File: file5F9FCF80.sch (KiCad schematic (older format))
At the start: 4 parts, among them J5 Conn_01x02, J6 Conn_01x02

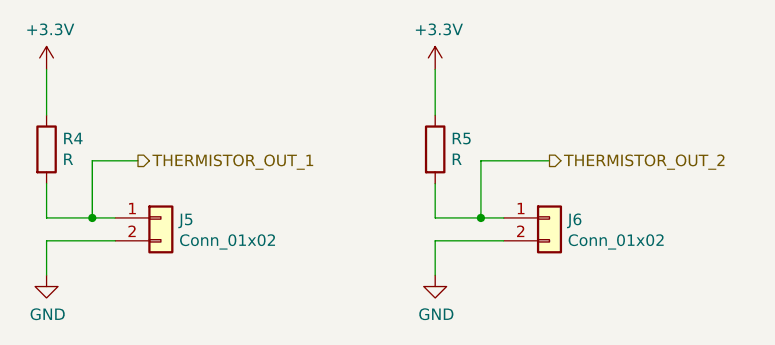
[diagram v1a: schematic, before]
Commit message: Added footprints
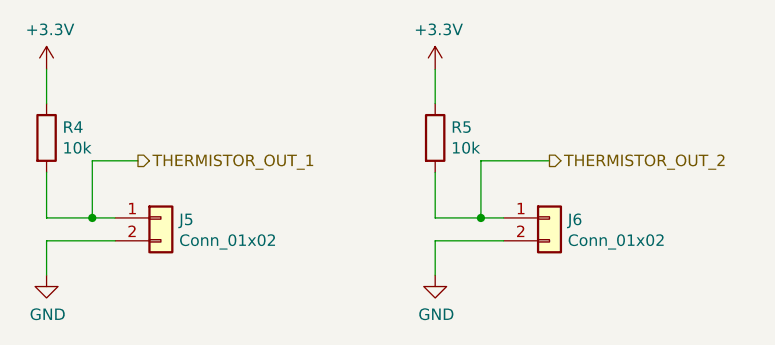
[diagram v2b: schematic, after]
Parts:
- J5, J6: footprint (none) -> Connector_PinHeader_2.54mm:PinHeader_1x02_P2.54mm_Vertical
- R4, R5: value R -> 10k; footprint (none) -> Resistor_SMD:R_0805_2012Metric
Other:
- moved on the sheet: R4, R5
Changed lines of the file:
@@
 L Device:R R4
 U 1 1 5F9FD435
-P 5150 2500
-F 0 "R4" H 5220 2546 50  0000 L CNN
-F 1 "R" H 5220 2455 50  0000 L CNN
-F 2 "" V 5080 2500 50  0001 C CNN
-F 3 "~" H 5150 2500 50  0001 C CNN
-	1    5150 2500
+P 5150 2450
+F 0 "R4" H 5220 2496 50  0000 L CNN
+F 1 "10k" H 5220 2405 50  0000 L CNN
+F 2 "Resistor_SMD:R_0805_2012Metric" V 5080 2450 50  0001 C CNN
+F 3 "~" H 5150 2450 50  0001 C CNN
+	1    5150 2450
 	1    0    0    -1
 $EndComp
 Wire Wire Line
-	5150 2150 5150 2350
+	5150 2150 5150 2300
 $Comp
 L Connector_Generic:Conn_01x02 J5
@@
 F 0 "J5" H 5730 2792 50  0000 L CNN
 F 1 "Conn_01x02" H 5730 2701 50  0000 L CNN
-F 2 "" H 5650 2800 50  0001 C CNN
+F 2 "Connector_PinHeader_2.54mm:PinHeader_1x02_P2.54mm_Vertical" H 5650 2800 50  0001 C CNN
 F 3 "~" H 5650 2800 50  0001 C CNN
 	1    5650 2800
@@
 	5450 2800 5350 2800
 Wire Wire Line
-	5150 2650 5150 2800
+	5150 2600 5150 2800
 $Comp
 L power:GND #PWR022
@@
 L Device:R R5
 U 1 1 5FA01CBA
-P 6850 2500
-F 0 "R5" H 6920 2546 50  0000 L CNN
-F 1 "R" H 6920 2455 50  0000 L CNN
-F 2 "" V 6780 2500 50  0001 C CNN
-F 3 "~" H 6850 2500 50  0001 C CNN
-	1    6850 2500
+P 6850 2450
+F 0 "R5" H 6920 2496 50  0000 L CNN
+F 1 "10k" H 6920 2405 50  0000 L CNN
+F 2 "Resistor_SMD:R_0805_2012Metric" V 6780 2450 50  0001 C CNN
+F 3 "~" H 6850 2450 50  0001 C CNN
+	1    6850 2450
 	1    0    0    -1
 $EndComp
 Wire Wire Line
-	6850 2150 6850 2350
+	6850 2150 6850 2300
 $Comp
 L Connector_Generic:Conn_01x02 J6
@@
 F 0 "J6" H 7430 2792 50  0000 L CNN
 F 1 "Conn_01x02" H 7430 2701 50  0000 L CNN
-F 2 "" H 7350 2800 50  0001 C CNN
+F 2 "Connector_PinHeader_2.54mm:PinHeader_1x02_P2.54mm_Vertical" H 7350 2800 50  0001 C CNN
 F 3 "~" H 7350 2800 50  0001 C CNN
 	1    7350 2800
@@
 	7150 2800 7050 2800
 Wire Wire Line
-	6850 2650 6850 2800
+	6850 2600 6850 2800
 $Comp
 L power:GND #PWR024
